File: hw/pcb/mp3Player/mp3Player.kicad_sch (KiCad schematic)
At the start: 0 parts

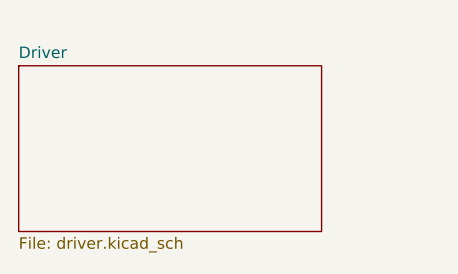
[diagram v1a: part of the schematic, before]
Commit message: updated pcb schematic
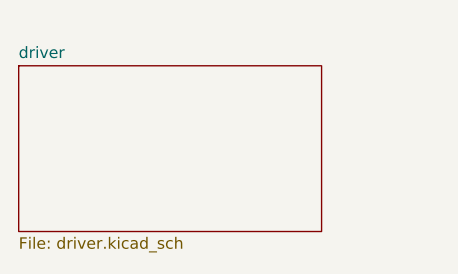
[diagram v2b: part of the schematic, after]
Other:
- sheet Driver renamed driver
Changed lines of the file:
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@@
 			(color 0 0 0 0)
 		)
-		(property "Sheetname" "Driver"
+		(property "Sheetname" "driver"
 			(at 41.91 62.1534 0)
 			(show_name no)

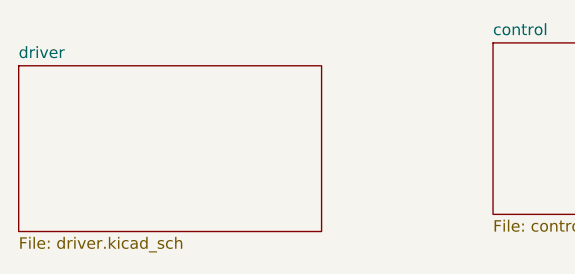
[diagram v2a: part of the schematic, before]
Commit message: updates to pcb to supported updated rtl
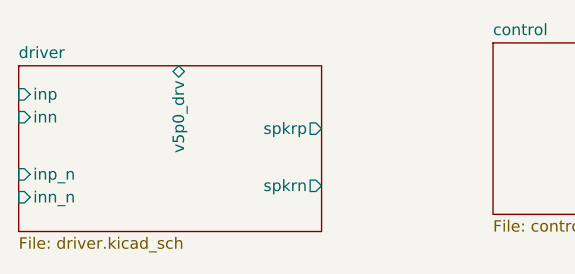
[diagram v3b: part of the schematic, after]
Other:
- sheet driver ports: added inn, inn_n, inp, inp_n, spkrn, spkrp, v5p0_drv; removed none
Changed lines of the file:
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@@
+			)
+		)
+		(pin "inn" input
+			(at 41.91 68.58 180)
+			(effects
+				(font
+					(size 1.27 1.27)
+				)
+				(justify left)
+			)
+		)
+		(pin "inn_n" input
+			(at 41.91 77.47 180)
+			(effects
+				(font
+					(size 1.27 1.27)
+				)
+				(justify left)
+			)
+		)
+		(pin "inp" input
+			(at 41.91 66.04 180)
+			(effects
+				(font
+					(size 1.27 1.27)
+				)
+				(justify left)
+			)
+		)
+		(pin "inp_n" input
+			(at 41.91 74.93 180)
+			(effects
+				(font
+					(size 1.27 1.27)
+				)
+				(justify left)
+			)
+		)
+		(pin "spkrn" output
+			(at 75.565 76.2 0)
+			(effects
+				(font
+					(size 1.27 1.27)
+				)
+				(justify right)
+			)
+		)
+		(pin "spkrp" output
+			(at 75.565 69.85 0)
+			(effects
+				(font
+					(size 1.27 1.27)
+				)
+				(justify right)
+			)
+		)
+		(pin "v5p0_drv" bidirectional
+			(at 59.69 62.865 90)
+			(effects
+				(font
+					(size 1.27 1.27)
+				)
+				(justify right)
 			)
 		)
